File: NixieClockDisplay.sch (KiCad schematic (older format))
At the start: 54 parts

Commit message: Begin board layout
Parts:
- removed LED? (x10): SK6812, symbol SK6812
- added LED1, LED10, LED2, LED3, LED4, LED5, LED6, LED7, LED8, LED9: SK6812MINI, NixieClockDisplay:LED_3535_4pin, symbol SK6812MINI
- C1, C10, C11, C12, C13, C14, C15, C16, C2, C3, C4, C5, C6, C7, C8, C9: renamed from C?; footprint (none) -> Capacitors_SMD:C_0805_HandSoldering
- N1, N2, N3, N4, N5, N6: renamed from N?; footprint (none) -> NixieClockDisplay:Socket_SK-136
- R1, R10, R11, R12, R13, R2, R3, R4, R5, R6, R7, R8, R9: renamed from R?; footprint (none) -> Resistors_SMD:R_0805_HandSoldering
- U1, U2, U3, U4, U5, U6: renamed from U?; footprint (none) -> Housings_SOIC:SOIC-20W_7.5x12.8mm_Pitch1.27mm
- U7: renamed from U?; footprint (none) -> NixieClockDisplay:WPMDL9500xx
- gave numbers to parts that had none: 2
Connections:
- wire segments 240 -> 241
- no-connect marks 18 -> 22

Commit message: Fiddling.
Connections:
- net labels added: HV
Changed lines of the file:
@@
 	1    0    0    -1
 $EndComp
+Text Label 9650 700  0    60   ~ 0
+HV
 $EndSCHEMATC

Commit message: More layout
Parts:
- added J2: CONN_01X03, Pin_Headers:Pin_Header_Angled_1x03_Pitch2.54mm, symbol CONN_01X03
- J1: footprint (none) -> Pin_Headers:Pin_Header_Angled_1x08_Pitch2.54mm
- J3: renamed from J2; footprint (none) -> Pin_Headers:Pin_Header_Angled_1x03_Pitch2.54mm
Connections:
- net labels added: SHDN
- net labels removed: DIN
- wire segments 241 -> 264
- no-connect marks 22 -> 19
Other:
- moved on the sheet: C1, C2, C3, C4, C5, C6, J1, N1, N2, N3, N4, N5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

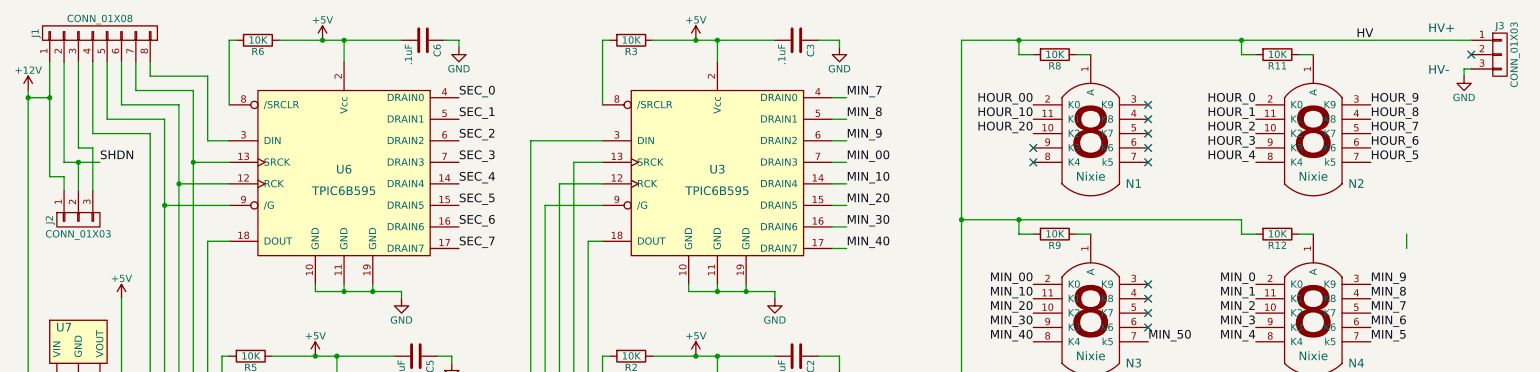
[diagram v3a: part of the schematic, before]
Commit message: Moved 5V bus.
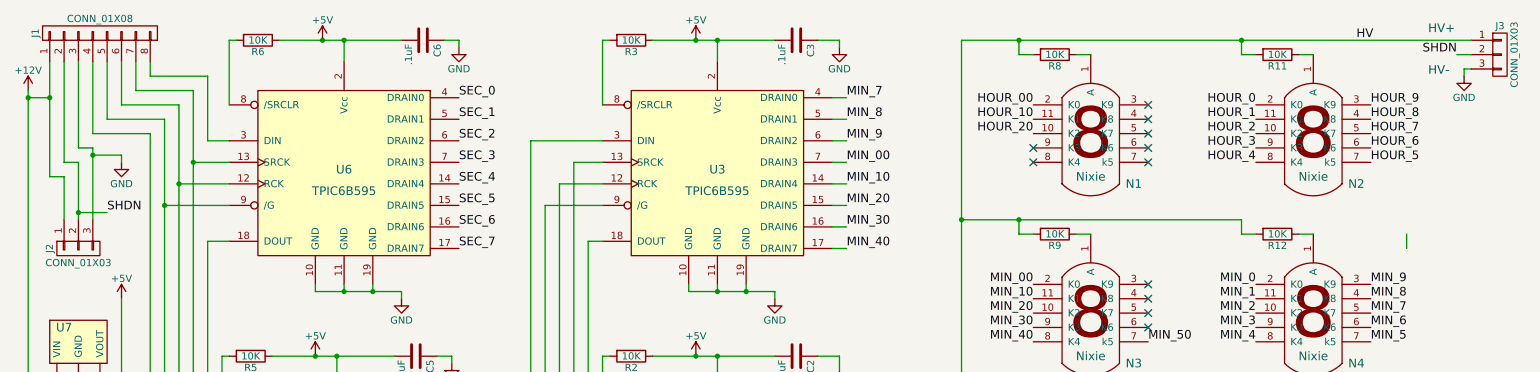
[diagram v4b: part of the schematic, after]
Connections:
- net GND: now also J1.3 (P3), J2.3 (P3)
- net SHDN: now also J3.2 (P2)
- no-connect marks 19 -> 18
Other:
- moved on the sheet: J2
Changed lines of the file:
@@
 	1    0    0    -1
 $EndComp
-NoConn ~ 10750 800
 $Comp
 L GND #PWR035
@@
 L CONN_01X03 J2
 U 1 1 593D18A5
-P 1050 1950
-F 0 "J2" H 1050 2150 50  0000 C CNN
-F 1 "CONN_01X03" V 1150 1950 50  0000 C CNN
-F 2 "Pin_Headers:Pin_Header_Angled_1x03_Pitch2.54mm" H 1050 1950 50  0001 C CNN
-F 3 "" H 1050 1950 50  0001 C CNN
-	1    1050 1950
+P 1050 2150
+F 0 "J2" H 1050 2350 50  0000 C CNN
+F 1 "CONN_01X03" V 1150 2150 50  0000 C CNN
+F 2 "Pin_Headers:Pin_Header_Angled_1x03_Pitch2.54mm" H 1050 2150 50  0001 C CNN
+F 3 "" H 1050 2150 50  0001 C CNN
+	1    1050 2150
 	0    -1   1    0
 $EndComp
@@
 	1050 1450 1150 1450
 Wire Wire Line
-	1150 1450 1150 1750
+	1150 1450 1150 1950
 Wire Wire Line
 	950  850  950  1550
 Wire Wire Line
-	950  1550 1200 1550
-Wire Wire Line
-	1050 1550 1050 1750
-Wire Wire Line
 	850  1650 950  1650
 Wire Wire Line
-	950  1650 950  1750
+	950  1650 950  1950
 Text Label 1250 4750 2    60   ~ 0
 SRCK
@@
 Wire Wire Line
 	1250 5200 1550 5200
-Text Label 1200 1550 0    60   ~ 0
+Text Label 1250 1900 0    60   ~ 0
 SHDN
-Connection ~ 1050 1550
 Wire Wire Line
 	2100 2100 1950 2100
@@
 Wire Wire Line
 	4700 5100 4750 5100
+Wire Wire Line
+	1050 1550 1050 1950
+Text Label 10650 800  2    60   ~ 0
+SHDN
+Wire Wire Line
+	10750 800  10650 800
+$Comp
+L GND #PWR?
+U 1 1 593F5D04
+P 1350 1550
+F 0 "#PWR?" H 1350 1300 50  0001 C CNN
+F 1 "GND" H 1350 1400 50  0000 C CNN
+F 2 "" H 1350 1550 50  0001 C CNN
+F 3 "" H 1350 1550 50  0001 C CNN
+	1    1350 1550
+	1    0    0    -1
+$EndComp
+Wire Wire Line
+	950  1550 1050 1550
+Wire Wire Line
+	1350 1550 1350 1500
+Wire Wire Line
+	1350 1500 1150 1500
+Connection ~ 1150 1500
+Wire Wire Line
+	1250 1900 1050 1900
+Connection ~ 1050 1900
 $EndSCHEMATC

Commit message: Routing complete
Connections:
- net SHDN: no longer J3.2 (P2)
- no-connect marks 18 -> 19
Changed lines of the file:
@@
 Wire Wire Line
 	1050 1550 1050 1950
-Text Label 10650 800  2    60   ~ 0
-SHDN
 Wire Wire Line
 	10750 800  10650 800
 $Comp
-L GND #PWR?
+L GND #PWR041
 U 1 1 593F5D04
 P 1350 1550
-F 0 "#PWR?" H 1350 1300 50  0001 C CNN
+F 0 "#PWR041" H 1350 1300 50  0001 C CNN
 F 1 "GND" H 1350 1400 50  0000 C CNN
 F 2 "" H 1350 1550 50  0001 C CNN
@@
 	1250 1900 1050 1900
 Connection ~ 1050 1900
+NoConn ~ 10650 800
 $EndSCHEMATC

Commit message: Added mounting holes
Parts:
- J1: footprint Pin_Headers:Pin_Header_Angled_1x08_Pitch2.54mm -> Pin_Headers:Pin_Header_Straight_1x08_Pitch2.54mm
- J2, J3: footprint Pin_Headers:Pin_Header_Angled_1x03_Pitch2.54mm -> Pin_Headers:Pin_Header_Straight_1x03_Pitch2.54mm
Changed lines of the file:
@@
 F 0 "J1" H 1200 1100 50  0000 C CNN
 F 1 "CONN_01X08" V 1300 650 50  0000 C CNN
-F 2 "Pin_Headers:Pin_Header_Angled_1x08_Pitch2.54mm" H 1200 650 50  0001 C CNN
+F 2 "Pin_Headers:Pin_Header_Straight_1x08_Pitch2.54mm" H 1200 650 50  0001 C CNN
 F 3 "" H 1200 650 50  0001 C CNN
 	1    1200 650
@@
 F 0 "J3" H 10950 1000 50  0000 C CNN
 F 1 "CONN_01X03" V 11050 800 50  0000 C CNN
-F 2 "Pin_Headers:Pin_Header_Angled_1x03_Pitch2.54mm" H 10950 800 50  0001 C CNN
+F 2 "Pin_Headers:Pin_Header_Straight_1x03_Pitch2.54mm" H 10950 800 50  0001 C CNN
 F 3 "" H 10950 800 50  0001 C CNN
 	1    10950 800
@@
 F 0 "J2" H 1050 2350 50  0000 C CNN
 F 1 "CONN_01X03" V 1150 2150 50  0000 C CNN
-F 2 "Pin_Headers:Pin_Header_Angled_1x03_Pitch2.54mm" H 1050 2150 50  0001 C CNN
+F 2 "Pin_Headers:Pin_Header_Straight_1x03_Pitch2.54mm" H 1050 2150 50  0001 C CNN
 F 3 "" H 1050 2150 50  0001 C CNN
 	1    1050 2150

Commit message: Finalized board
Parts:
- added J4: CONN_02X04, Pin_Headers:Pin_Header_Straight_2x04_Pitch2.54mm, symbol CONN_02X04
- added J5: CONN_01X02, Pin_Headers:Pin_Header_Straight_1x02_Pitch2.54mm, symbol CONN_01X02
- renumbered R9 to R10, R12 to R11, R10 to R12, R11 to R9
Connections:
- net +5V: now also J4.7 (P7), J5.1 (P1)
- net GND: now also J4.8 (P8), J5.2 (P2)
- net PIXEL_IN: now also J4.1 (P1); no longer R7.2
- new net: J4.2 (P2), R7.2
- new net RING_IN: J4.4 (P4), J4.6 (P6)
- new net RING_OUT: J4.3 (P3), J4.5 (P5)
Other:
- moved on the sheet: U7

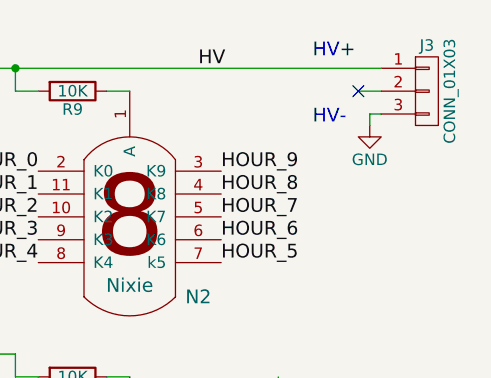
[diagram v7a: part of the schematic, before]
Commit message: Arranged connectors to mate with NixiePowerSupply board.
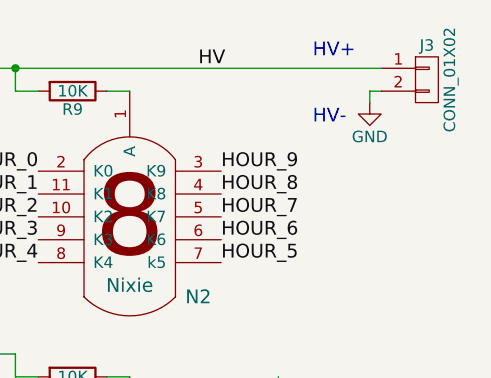
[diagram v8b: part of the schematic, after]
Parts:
- removed J3: CONN_01X03, Pin_Headers:Pin_Header_Straight_1x03_Pitch2.54mm, symbol CONN_01X03
- added J3: CONN_01X02, NixieClockDisplay:Pin_Header_Straight_1x03_Pitch2.54mm_No_Center, symbol CONN_01X02
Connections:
- net GND: now also J3.2 (P2)
- net HV: now also J3.1 (P1)
- no-connect marks 19 -> 18
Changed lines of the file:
@@
-$EndComp
-$Comp
-L CONN_01X03 J3
-U 1 1 59345D10
-P 10950 800
-F 0 "J3" H 10950 1000 50  0000 C CNN
-F 1 "CONN_01X03" V 11050 800 50  0000 C CNN
-F 2 "Pin_Headers:Pin_Header_Straight_1x03_Pitch2.54mm" H 10950 800 50  0001 C CNN
-F 3 "" H 10950 800 50  0001 C CNN
-	1    10950 800
-	1    0    0    -1
 $EndComp
 $Comp
 L GND #PWR035
 U 1 1 593464D5
-P 10700 950
-F 0 "#PWR035" H 10700 700 50  0001 C CNN
-F 1 "GND" H 10700 800 50  0000 C CNN
-F 2 "" H 10700 950 50  0001 C CNN
-F 3 "" H 10700 950 50  0001 C CNN
-	1    10700 950
+P 10700 850
+F 0 "#PWR035" H 10700 600 50  0001 C CNN
+F 1 "GND" H 10700 700 50  0000 C CNN
+F 2 "" H 10700 850 50  0001 C CNN
+F 3 "" H 10700 850 50  0001 C CNN
+	1    10700 850
 	1    0    0    -1
 $EndComp
@@
 	1    0    0    -1
 $EndComp
-NoConn ~ 10650 800
 $Comp
 L CONN_02X04 J4
@@
 	1150 850  1150 1350
 Connection ~ 9150 700
-Wire Wire Line
-	10700 950  10700 900
-Wire Wire Line
-	10700 900  10750 900
 Wire Wire Line
 	1150 7300 1150 7450
@@
 	1050 1550 1050 1950
 Wire Wire Line
-	10750 800  10650 800
-Wire Wire Line
 	950  1550 1050 1550
 Wire Wire Line
@@
 Wire Wire Line
 	800  4350 800  4400
+$Comp
+L CONN_01X02 J3
+U 1 1 5947052E
+P 10950 750
+F 0 "J3" H 10950 900 50  0000 C CNN
+F 1 "CONN_01X02" V 11050 750 50  0000 C CNN
+F 2 "NixieClockDisplay:Pin_Header_Straight_1x03_Pitch2.54mm_No_Center" H 10950 750 50  0001 C CNN
+F 3 "" H 10950 750 50  0001 C CNN
+	1    10950 750
+	1    0    0    -1
+$EndComp
+Wire Wire Line
+	10700 850  10700 800
+Wire Wire Line
+	10700 800  10750 800
 $EndSCHEMATC
